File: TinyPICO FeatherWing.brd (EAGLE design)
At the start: 50.8 x 22.9 mm, 4 parts

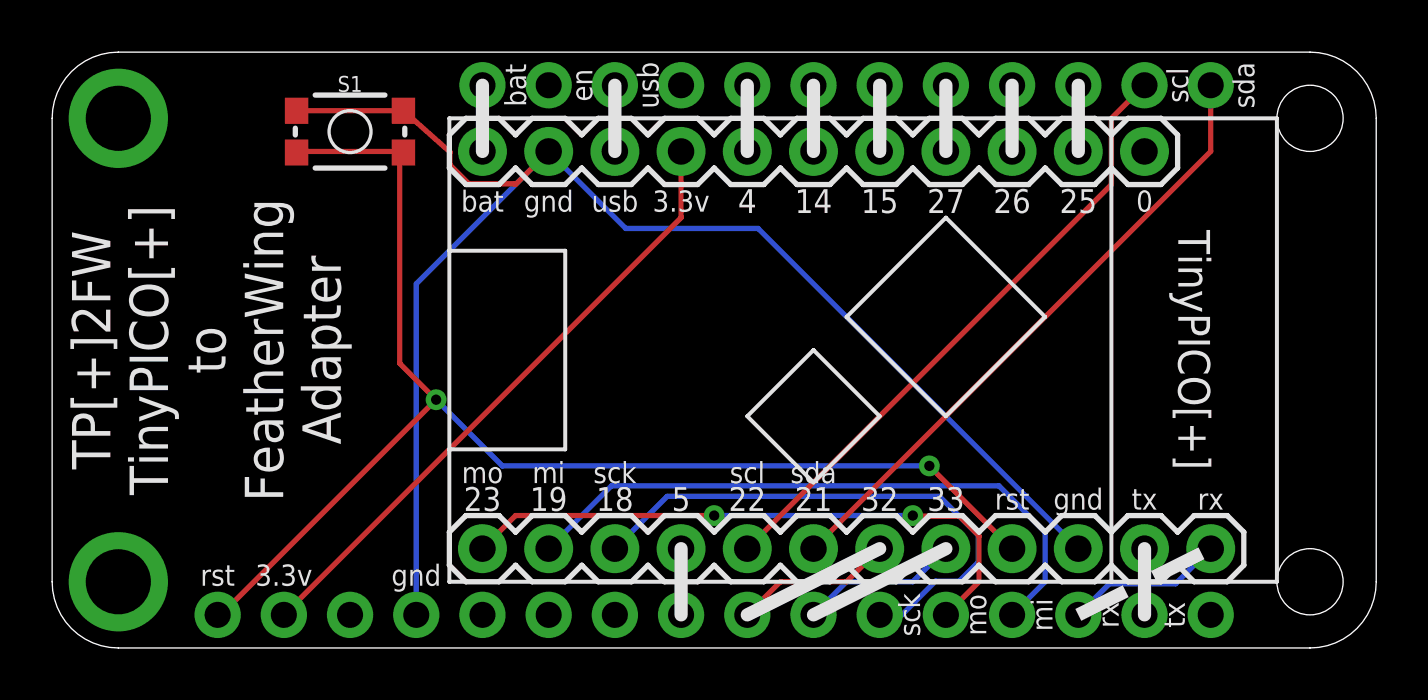
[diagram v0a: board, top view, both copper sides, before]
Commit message: Tiny tweak to Reset trace
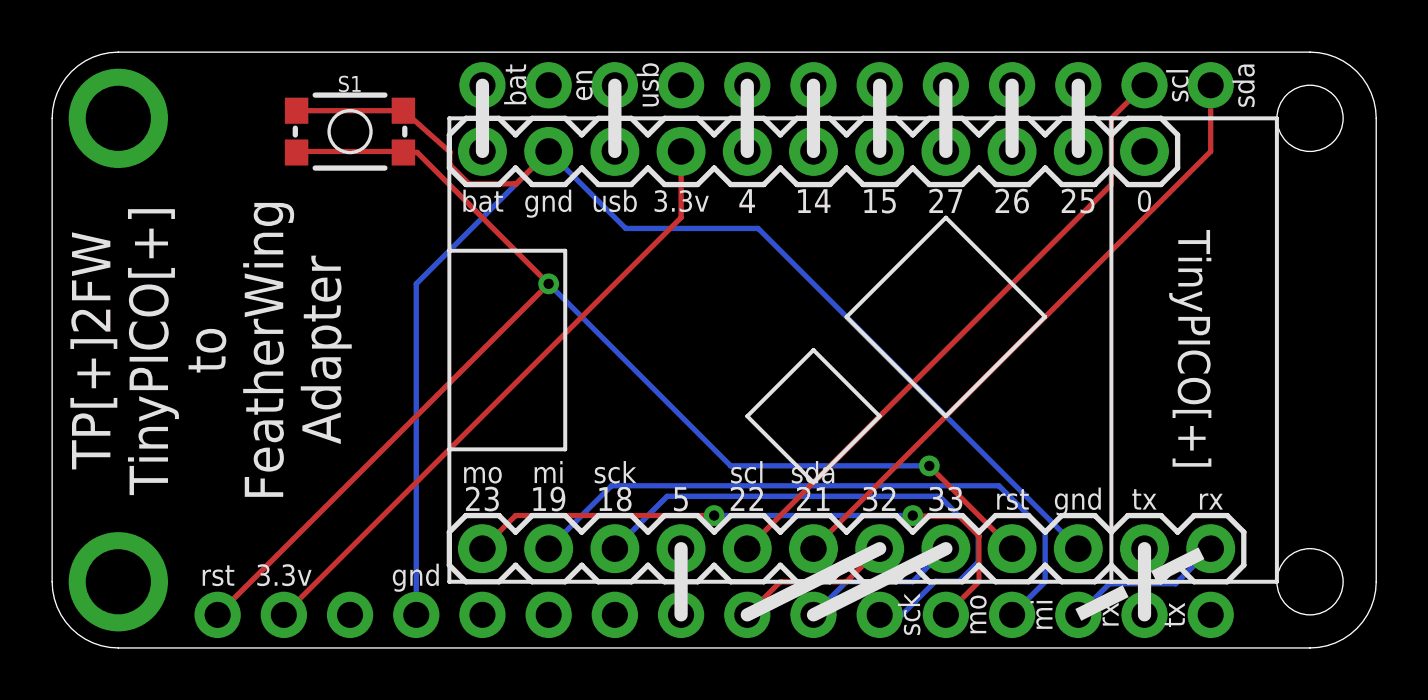
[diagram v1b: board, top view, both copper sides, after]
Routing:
- net RESET: track 50.5 -> 51.7 mm
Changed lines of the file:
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@@
 <layer number="14" name="Route14" color="1" fill="6" visible="no" active="no"/>
 <layer number="15" name="Route15" color="4" fill="6" visible="no" active="no"/>
-<layer number="16" name="Bottom" color="1" fill="1" visible="no" active="yes"/>
+<layer number="16" name="Bottom" color="1" fill="1" visible="yes" active="yes"/>
 <layer number="17" name="Pads" color="2" fill="1" visible="yes" active="yes"/>
 <layer number="18" name="Vias" color="2" fill="1" visible="yes" active="yes"/>
@@
 <wire x1="13.335" y1="19.05" x2="9.525" y2="19.05" width="0.2032" layer="1"/>
 <wire x1="9.525" y1="19.05" x2="9.38" y2="19.012" width="0.2032" layer="1"/>
-<wire x1="17.272" y1="6.985" x2="33.655" y2="6.985" width="0.2032" layer="16"/>
-<wire x1="14.732" y1="9.525" x2="17.272" y2="6.985" width="0.2032" layer="16"/>
-<wire x1="13.335" y1="10.922" x2="14.732" y2="9.525" width="0.2032" layer="1"/>
-<wire x1="13.335" y1="19.05" x2="13.335" y2="10.922" width="0.2032" layer="1"/>
+<wire x1="26.035" y1="6.985" x2="33.655" y2="6.985" width="0.2032" layer="16"/>
+<wire x1="19.05" y1="13.97" x2="26.035" y2="6.985" width="0.2032" layer="16"/>
+<wire x1="13.48" y1="19.012" x2="14.008" y2="19.012" width="0.2032" layer="1"/>
+<wire x1="19.05" y1="13.97" x2="14.008" y2="19.012" width="0.2032" layer="1"/>
 <wire x1="13.335" y1="19.05" x2="13.48" y2="19.012" width="0.2032" layer="1"/>
 <via x="33.655" y="6.985" extent="1-16" drill="0.3937"/>
-<via x="14.732" y="9.525" extent="1-16" drill="0.3937"/>
+<via x="19.05" y="13.97" extent="1-16" drill="0.3937"/>
 <wire x1="36.83" y1="3.81" x2="33.655" y2="6.985" width="0.2032" layer="1"/>
-<wire x1="6.35" y1="1.27" x2="6.477" y2="1.27" width="0.2032" layer="1"/>
-<wire x1="14.732" y1="9.525" x2="6.477" y2="1.27" width="0.2032" layer="1"/>
+<wire x1="6.35" y1="1.27" x2="19.05" y2="13.97" width="0.2032" layer="1"/>
 </signal>
 <signal name="GPIO32">
